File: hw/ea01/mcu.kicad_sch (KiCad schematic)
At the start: 44 parts, among them J2 USB_B, J3 Conn_01x05_Pin, J8 Conn_01x03_Pin, J9 Conn_01x03_Pin, SW1 SW_Push, SW2 SW_Push, U1 RP2040, U11 W25Q32JVSS, U3 NUP2202, Y1 12Mhz

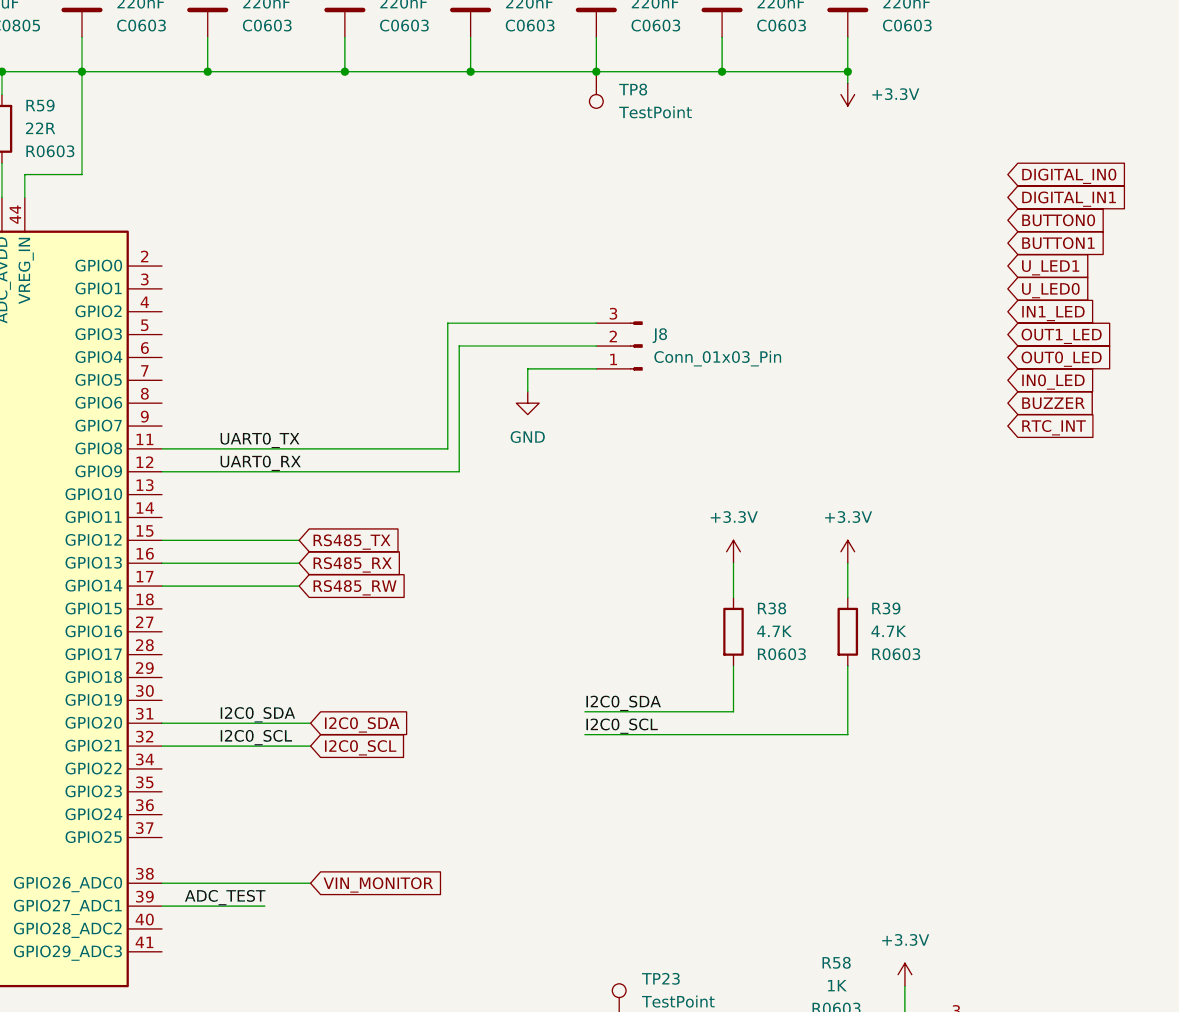
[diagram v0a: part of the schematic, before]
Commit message: errors fix for comp fp
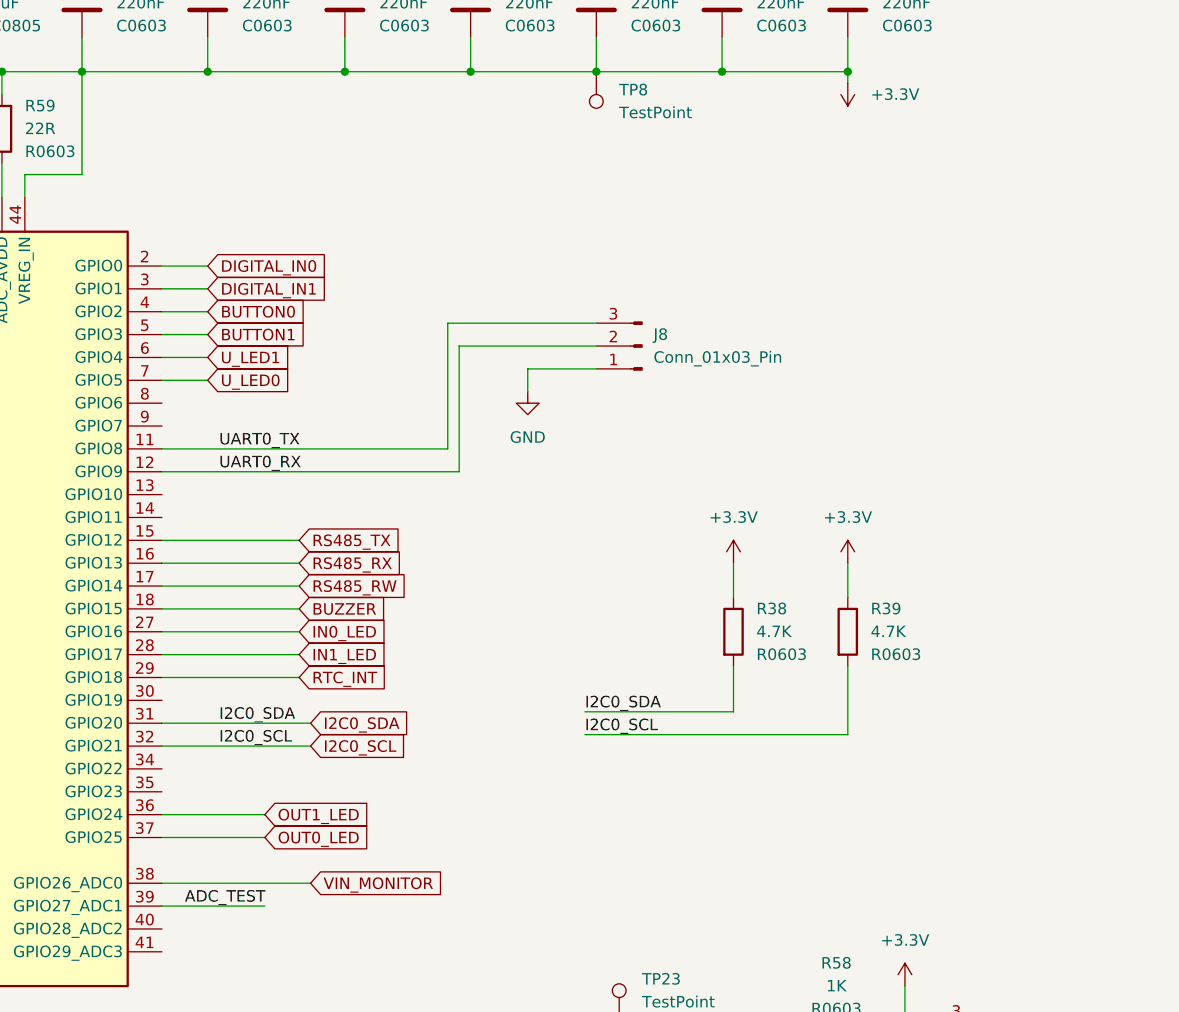
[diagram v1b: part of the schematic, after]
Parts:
- FB1, FB2, FB3: footprint (none) -> Resistor_SMD:R_0805_2012Metric
- J2: footprint (none) -> Connector_USB:USB_B_OST_USB-B1HSxx_Horizontal
- J3: footprint (none) -> Connector_PinHeader_2.54mm:PinHeader_1x05_P2.54mm_Vertical
- J8, J9: footprint (none) -> Connector_PinHeader_2.54mm:PinHeader_1x03_P2.54mm_Vertical
- SW1, SW2: footprint Button_Switch_THT:SW_Tactile_SPST_Angled_PTS645Vx58-2LFS -> Button_Switch_THT:SW_PUSH_6mm_H5mm
- Y1: footprint (none) -> Crystal:Crystal_SMD_Abracon_ABM3-2Pin_5.0x3.2mm
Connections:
- net BUTTON0: now also U1.4 (GPIO2)
- net BUTTON1: now also U1.5 (GPIO3)
- net BUZZER: now also U1.18 (GPIO15)
- net DIGITAL_IN0: now also U1.2 (GPIO0)
- net DIGITAL_IN1: now also U1.3 (GPIO1)
- net IN0_LED: now also U1.27 (GPIO16)
- net IN1_LED: now also U1.28 (GPIO17)
- net OUT0_LED: now also U1.37 (GPIO25)
- net OUT1_LED: now also U1.36 (GPIO24)
- net RTC_INT: now also U1.29 (GPIO18)
- net U_LED0: now also U1.7 (GPIO5)
- net U_LED1: now also U1.6 (GPIO4)

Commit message: pcb drawing continue..
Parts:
- added C63: 100nF, Capacitor_SMD:C_0603_1608Metric, symbol Device:C
- added R81, R82, R83, R84: 4.7K, Resistor_SMD:R_0603_1608Metric, symbol Device:R
- SW1, SW2: footprint Button_Switch_THT:SW_PUSH_6mm_H5mm -> Button_Switch_THT:SW_Tactile_SPST_Angled_PTS645Vx83-2LFS
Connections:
- net +3.3V: now also R81.1, R83.1
- net GND: now also C63.2, R82.2, R84.2
- net HW_ADDRESS: now reaches U1.41 (GPIO29_ADC3)
- net HW_ADDRESS: now also C63.1, R81.2, R82.1
- net HW_VERSION: now reaches U1.8 (GPIO6)
- net HW_VERSION: now also R83.2, R84.1
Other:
- moved on the sheet: C1, J8, R1, SW1, TP7

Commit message: component placement continue..
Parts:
- removed TP23, TP6, TP7: TestPoint, TestPoint:TestPoint_Pad_D1.5mm, symbol Connector:TestPoint
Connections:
- net OUT1: now reaches U1.34 (GPIO22)
- net OUT0: now reaches U1.35 (GPIO23)
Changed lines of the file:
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@@
 	)
 	(junction
-		(at 113.03 36.83)
-		(diameter 0)
-		(color 0 0 0 0)
-	)
-	(junction
 		(at 234.95 35.56)
 		(diameter 0)
@@
 	)
 	(junction
-		(at 102.87 168.91)
-		(diameter 0)
-		(color 0 0 0 0)
-	)
-	(junction
 		(at 220.98 35.56)
 		(diameter 0)
@@
 	(wire
 		(pts
-			(xy 223.52 140.97) (xy 223.52 143.51)
-		)
-		(stroke
-			(width 0)
-			(type default)
-		)
-	)
-	(wire
-		(pts
 			(xy 106.68 85.09) (xy 121.92 85.09)
 		)
@@
 	(wire
 		(pts
+			(xy 172.72 115.57) (xy 184.15 115.57)
+		)
+		(stroke
+			(width 0)
+			(type default)
+		)
+	)
+	(wire
+		(pts
 			(xy 102.87 168.91) (xy 116.84 168.91)
 		)
@@
 	(wire
 		(pts
+			(xy 172.72 113.03) (xy 184.15 113.03)
+		)
+		(stroke
+			(width 0)
+			(type default)
+		)
+	)
+	(wire
+		(pts
 			(xy 25.4 134.62) (xy 25.4 132.08)
 		)
@@
 		)
 	)
+	(global_label "OUT1"
+		(shape input)
+		(at 184.15 113.03 0)
+		(fields_autoplaced yes)
+		(effects
+			(font
+				(size 1.27 1.27)
+			)
+			(justify left)
+		)
+		(property "Intersheetrefs" "${INTERSHEET_REFS}"
+			(at 191.9733 113.03 0)
+			(effects
+				(font
+					(size 1.27 1.27)
+				)
+				(justify left)
+				(hide yes)
+			)
+		)
+	)
 	(global_label "OUT1_LED"
 		(shape input)
@@
 		)
 	)
+	(global_label "OUT0"
+		(shape input)
+		(at 184.15 115.57 0)
+		(fields_autoplaced yes)
+		(effects
+			(font
+				(size 1.27 1.27)
+			)
+			(justify left)
+		)
+		(property "Intersheetrefs" "${INTERSHEET_REFS}"
+			(at 191.9733 115.57 0)
+			(effects
+				(font
+					(size 1.27 1.27)
+				)
+				(justify left)
+				(hide yes)
+			)
+		)
+	)
 	(global_label "I2C0_SDA"
 		(shape input)
@@
 	)
 	(symbol
-		(lib_id "Connector:TestPoint")
-		(at 223.52 140.97 0)
-		(unit 1)
-		(exclude_from_sim no)
-		(in_bom yes)
-		(on_board yes)
-		(dnp no)
-		(fields_autoplaced yes)
-		(property "Reference" "TP23"
-			(at 226.06 136.3979 0)
-			(effects
-				(font
-					(size 1.27 1.27)
-				)
-				(justify left)
-			)
-		)
-		(property "Value" "TestPoint"
-			(at 226.06 138.9379 0)
-			(effects
-				(font
-					(size 1.27 1.27)
-				)
-				(justify left)
-			)
-		)
-		(property "Footprint" "TestPoint:TestPoint_Pad_D1.5mm"
-			(at 228.6 140.97 0)
-			(effects
-				(font
-					(size 1.27 1.27)
-				)
-				(hide yes)
-			)
-		)
-		(property "Datasheet" "~"
-			(at 228.6 140.97 0)
-			(effects
-				(font
-					(size 1.27 1.27)
-				)
-				(hide yes)
-			)
-		)
-		(property "Description" "test point"
-			(at 223.52 140.97 0)
-			(effects
-				(font
-					(size 1.27 1.27)
-				)
-				(hide yes)
-			)
-		)
-		(pin "1"
-		)
-		(instances
-			(project "ea01"
-				(path "/1c1d47d5-f6ab-48f4-aef9-e333cdfe2713/d3810c5d-87fe-4ffb-a7ba-b811c8939351"
-					(reference "TP23")
-					(unit 1)
-				)
-			)
-		)
-	)
-	(symbol
 		(lib_id "Device:FerriteBead")
 		(at 21.59 50.8 0)
@@
 	)
 	(symbol
-		(lib_id "Connector:TestPoint")
-		(at 102.87 168.91 0)
-		(unit 1)
-		(exclude_from_sim no)
-		(in_bom yes)
-		(on_board yes)
-		(dnp no)
-		(fields_autoplaced yes)
-		(property "Reference" "TP7"
-			(at 105.41 164.3379 0)
-			(effects
-				(font
-					(size 1.27 1.27)
-				)
-				(justify left)
-			)
-		)
-		(property "Value" "TestPoint"
-			(at 105.41 166.8779 0)
-			(effects
-				(font
-					(size 1.27 1.27)
-				)
-				(justify left)
-			)
-		)
-		(property "Footprint" "TestPoint:TestPoint_Pad_D1.5mm"
-			(at 107.95 168.91 0)
-			(effects
-				(font
-					(size 1.27 1.27)
-				)
-				(hide yes)
-			)
-		)
-		(property "Datasheet" "~"
-			(at 107.95 168.91 0)
-			(effects
-				(font
-					(size 1.27 1.27)
-				)
-				(hide yes)
-			)
-		)
-		(property "Description" "test point"
-			(at 102.87 168.91 0)
-			(effects
-				(font
-					(size 1.27 1.27)
-				)
-				(hide yes)
-			)
-		)
-		(pin "1"
-		)
-		(instances
-			(project "ea01"
-				(path "/1c1d47d5-f6ab-48f4-aef9-e333cdfe2713/d3810c5d-87fe-4ffb-a7ba-b811c8939351"
-					(reference "TP7")
-					(unit 1)
-				)
-			)
-		)
-	)
-	(symbol
 		(lib_id "Device:R")
 		(at 25.4 160.02 0)
@@
 					(unit 1)
 				)
-			)
-		)
-	)
-	(symbol
-		(lib_id "Connector:TestPoint")
-		(at 113.03 36.83 0)
-		(unit 1)
-		(exclude_from_sim no)
-		(in_bom yes)
-		(on_board yes)
-		(dnp no)
-		(fields_autoplaced yes)
-		(property "Reference" "TP6"
-			(at 115.57 32.2579 0)
-			(effects
-				(font
-					(size 1.27 1.27)
-				)
-				(justify left)
-			)
-		)
-		(property "Value" "TestPoint"
-			(at 115.57 34.7979 0)
-			(effects
-				(font
-					(size 1.27 1.27)
-				)
-				(justify left)
-			)
-		)
-		(property "Footprint" "TestPoint:TestPoint_Pad_D1.5mm"
-			(at 118.11 36.83 0)
-			(effects
-				(font
-					(size 1.27 1.27)
-				)
-				(hide yes)
-			)
-		)
-		(property "Datasheet" "~"
-			(at 118.11 36.83 0)
-			(effects
-				(font
-					(size 1.27 1.27)
-				)
-				(hide yes)
-			)
-		)
-		(property "Description" "test point"
-			(at 113.03 36.83 0)
-			(effects
-				(font
-					(size 1.27 1.27)
-				)
-				(hide yes)
-			)
-		)
-		(pin "1"
-		)
-		(instances
-			(project "ea01"
-				(path "/1c1d47d5-f6ab-48f4-aef9-e333cdfe2713/d3810c5d-87fe-4ffb-a7ba-b811c8939351"
-					(reference "TP6")
-					(unit 1)
-				)

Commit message: placement continue...
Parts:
- removed TP8: TestPoint, TestPoint:TestPoint_Pad_D1.5mm, symbol Connector:TestPoint
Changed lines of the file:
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@@
-	)
-	(symbol
-		(lib_id "Connector:TestPoint")
-		(at 220.98 35.56 180)
-		(unit 1)
-		(exclude_from_sim no)
-		(in_bom yes)
-		(on_board yes)
-		(dnp no)
-		(fields_autoplaced yes)
-		(property "Reference" "TP8"
-			(at 223.52 37.5919 0)
-			(effects
-				(font
-					(size 1.27 1.27)
-				)
-				(justify right)
-			)
-		)
-		(property "Value" "TestPoint"
-			(at 223.52 40.1319 0)
-			(effects
-				(font
-					(size 1.27 1.27)
-				)
-				(justify right)
-			)
-		)
-		(property "Footprint" "TestPoint:TestPoint_Pad_D1.5mm"
-			(at 215.9 35.56 0)
-			(effects
-				(font
-					(size 1.27 1.27)
-				)
-				(hide yes)
-			)
-		)
-		(property "Datasheet" "~"
-			(at 215.9 35.56 0)
-			(effects
-				(font
-					(size 1.27 1.27)
-				)
-				(hide yes)
-			)
-		)
-		(property "Description" "test point"
-			(at 220.98 35.56 0)
-			(effects
-				(font
-					(size 1.27 1.27)
-				)
-				(hide yes)
-			)
-		)
-		(pin "1"
-		)
-		(instances
-			(project "ea01"
-				(path "/1c1d47d5-f6ab-48f4-aef9-e333cdfe2713/d3810c5d-87fe-4ffb-a7ba-b811c8939351"
-					(reference "TP8")
-					(unit 1)
-				)
-			)
-		)
 	)
 	(symbol

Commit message: placement optimization and review continue
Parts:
- added R7, R8: 4.7K, Resistor_SMD:R_0603_1608Metric, symbol Device:R
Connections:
- net +3.3V: now also R7.1
- net GND: now also R8.2
- net HW_VER1: now reaches U1.9 (GPIO7)
- net HW_VER1: now also R7.2, R8.1
- net HW_VERSION renamed HW_VER0

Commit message: drawing continue...
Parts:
- removed U3: NUP2202, Package_TO_SOT_SMD:SOT-363_SC-70-6, symbol Power_Protection:NUP2202
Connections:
- net GND: now also SW1.2; no longer SW1.1
- net RUN: now also SW1.1; no longer SW1.2
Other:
- moved on the sheet: SW1

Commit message: drawing continue...
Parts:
- removed C60: 100nF, Capacitor_SMD:C_0603_1608Metric, symbol Device:C
- removed C61: 22pF, Capacitor_SMD:C_0603_1608Metric, symbol Device:C
- removed J9: Conn_01x03_Pin, Connector_PinHeader_2.54mm:PinHeader_1x03_P2.54mm_Vertical, symbol Connector:Conn_01x03_Pin
- removed R58: 1K, Resistor_SMD:R_0603_1608Metric, symbol Device:R
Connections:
- net VIN_MONITOR is gone; now on net HW_ADDRESS: U1.38 (GPIO26_ADC0)
- net HW_ADDRESS: no longer U1.41 (GPIO29_ADC3)
- net OUT0_LED: now also U1.14 (GPIO11); no longer U1.37 (GPIO25)
- net OUT1_LED: now also U1.13 (GPIO10); no longer U1.36 (GPIO24)
- net ADC_TEST: no longer names the net of U1.39 (GPIO27_ADC1)

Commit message: drawing continue..
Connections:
- net BUZZER: no longer names the net of U1.18 (GPIO15)
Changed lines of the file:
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@@
-	(wire
-		(pts
-			(xy 172.72 95.25) (xy 187.96 95.25)
-		)
-		(stroke
-			(width 0)
-			(type default)
-		)
-	)
 	(wire
 		(pts
@@
 			(effects
 				(font
-					(size 1.27 1.27)
-				)
-				(justify left)
-				(hide yes)
-			)
-		)
-	)
-	(global_label "BUZZER"
-		(shape input)
-		(at 187.96 95.25 0)
-		(fields_autoplaced yes)
-		(effects
-			(font
-				(size 1.27 1.27)
-			)
-			(justify left)
-		)
-		(property "Intersheetrefs" "${INTERSHEET_REFS}"
-			(at 198.3837 95.25 0)
-			(effects
-				(font
